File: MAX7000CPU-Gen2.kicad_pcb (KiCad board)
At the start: 2 copper layers, 109 parts, among them J1 Conn_02x05_Odd_Even, J2 Conn_01x08_Male, J4 Conn_01x08_Male, J5 Conn_01x08_Male, J7 Conn_01x05_Male, SW1 SW_Push, SW2 SW_Push, SW3 SW_Push, U1 NE555P, U10 CD4029BEE4, U11 CD4029BEE4, U12 CD4029BEE4, U13 74LS241, U14 74LS241, U15 74LS241, U16 74LS241, U17 74LS574, U18 74LS574, U19 AS6C1008-55PCN, U2 NE555P, U20 74LS574, U21 CD4029BEE4, U22 CD4029BEE4, U23 CD4029BEE4, U24 CD4029BEE4, U25 74LS241, U26 74LS241, U28 74LS574, U29 EPM7128slc84-15n, U3 NE555P, U4 74LS574, U5 74LS574, U6 74LS574, U7 74LS574, U8 74LS574, U9 CD4029BEE4

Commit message: Counter Layout
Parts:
- removed the R2 at (122.0, 28.8)
- removed the U1 at (69.5, 71.1)
- removed the U8 at (20.4, 55.1)
- added R10: 50K, Resistor_THT:R_Axial_DIN0207_L6.3mm_D2.5mm_P7.62mm_Horizontal, F.Cu at (141.8, 78.0)
- added R11: 50K, Resistor_THT:R_Axial_DIN0207_L6.3mm_D2.5mm_P7.62mm_Horizontal, F.Cu at (348.2, 78.0)
- added R12: 50K, Resistor_THT:R_Axial_DIN0207_L6.3mm_D2.5mm_P7.62mm_Horizontal, F.Cu at (335.8, 66.0)
- added R13: 50K, Resistor_THT:R_Axial_DIN0207_L6.3mm_D2.5mm_P7.62mm_Horizontal, F.Cu at (131.1, 90.1)
- added R14: 50K, Resistor_THT:R_Axial_DIN0207_L6.3mm_D2.5mm_P7.62mm_Horizontal, F.Cu at (152.6, 78.0)
- added R15: 50K, Resistor_THT:R_Axial_DIN0207_L6.3mm_D2.5mm_P7.62mm_Horizontal, F.Cu at (376.7, 103.1)
- added R28: 50K, Resistor_THT:R_Axial_DIN0207_L6.3mm_D2.5mm_P7.62mm_Horizontal, F.Cu at (336.6, 95.0)
- added R29: 50K, Resistor_THT:R_Axial_DIN0207_L6.3mm_D2.5mm_P7.62mm_Horizontal, F.Cu at (376.4, 65.8)
- added R30: 50K, Resistor_THT:R_Axial_DIN0207_L6.3mm_D2.5mm_P7.62mm_Horizontal, F.Cu at (141.8, 90.1)
- added R31: 50K, Resistor_THT:R_Axial_DIN0207_L6.3mm_D2.5mm_P7.62mm_Horizontal, F.Cu at (376.4, 94.2)
- added R32: 50K, Resistor_THT:R_Axial_DIN0207_L6.3mm_D2.5mm_P7.62mm_Horizontal, F.Cu at (376.4, 83.8)
- added R33: 50K, Resistor_THT:R_Axial_DIN0207_L6.3mm_D2.5mm_P7.62mm_Horizontal, F.Cu at (141.8, 94.2)
- added R34: 50K, Resistor_THT:R_Axial_DIN0207_L6.3mm_D2.5mm_P7.62mm_Horizontal, F.Cu at (152.6, 86.1)
- added R35: 50K, Resistor_THT:R_Axial_DIN0207_L6.3mm_D2.5mm_P7.62mm_Horizontal, F.Cu at (163.4, 82.0)
- added R36: 50K, Resistor_THT:R_Axial_DIN0207_L6.3mm_D2.5mm_P7.62mm_Horizontal, F.Cu at (152.6, 90.1)
- added R37: 50K, Resistor_THT:R_Axial_DIN0207_L6.3mm_D2.5mm_P7.62mm_Horizontal, F.Cu at (141.8, 98.2)
- added R38: 50K, Resistor_THT:R_Axial_DIN0207_L6.3mm_D2.5mm_P7.62mm_Horizontal, F.Cu at (152.6, 94.2)
- added R39: 50K, Resistor_THT:R_Axial_DIN0207_L6.3mm_D2.5mm_P7.62mm_Horizontal, F.Cu at (152.6, 98.2)
- added R40: 50K, Resistor_THT:R_Axial_DIN0207_L6.3mm_D2.5mm_P7.62mm_Horizontal, F.Cu at (163.4, 86.1)
- added R41: 50K, Resistor_THT:R_Axial_DIN0207_L6.3mm_D2.5mm_P7.62mm_Horizontal, F.Cu at (163.4, 90.1)
- added R42: 50K, Resistor_THT:R_Axial_DIN0207_L6.3mm_D2.5mm_P7.62mm_Horizontal, F.Cu at (359.2, 78.0)
- added R43: 50K, Resistor_THT:R_Axial_DIN0207_L6.3mm_D2.5mm_P7.62mm_Horizontal, F.Cu at (358.9, 118.1)
- added R6: 1K, Resistor_THT:R_Axial_DIN0207_L6.3mm_D2.5mm_P7.62mm_Horizontal, F.Cu at (341.6, 51.8)
- added R8: 50K, Resistor_THT:R_Axial_DIN0207_L6.3mm_D2.5mm_P7.62mm_Horizontal, F.Cu at (131.1, 78.0)
- added R9: 50K, Resistor_THT:R_Axial_DIN0207_L6.3mm_D2.5mm_P7.62mm_Horizontal, F.Cu at (131.1, 82.0)
- added RV1: 1M, MAX7000CPU:SIP460W50P254L970H980Q3P, F.Cu at (328.4, 58.4)
- added U15: 74LS574, Package_DIP:DIP-20_W7.62mm, F.Cu at (324.4, 95.0)
- added U2: NE555P, Package_DIP:DIP-8_W7.62mm, F.Cu at (324.4, 44.4)
- moved U19 368.7 mm to (398.0, 96.8), turned to 180 degrees
- moved U10 318.2 mm to (364.5, 66.0)
- moved U16 306.1 mm to (364.7, 95.0)
- moved C1 303.6 mm to (394.5, 52.5), turned to 90 degrees
- moved U7 297.4 mm to (340.9, 73.4), turned to 90 degrees
- moved C2 297.4 mm to (394.5, 44.2), turned to 270 degrees
- moved R2 286.6 mm to (399.3, 44.7), turned to 270 degrees
- moved U13 284.8 mm to (341.4, 89.9), turned to 90 degrees
- moved C17 279.3 mm to (376.4, 98.8), turned to 270 degrees
- moved C4 277.6 mm to (368.0, 44.2), turned to 270 degrees
- moved R4 275.9 mm to (377.7, 52.3), turned to 90 degrees
- moved U14 272.8 mm to (341.4, 102.4), turned to 90 degrees
- moved SW3 269.9 mm to (372.1, 56.4)
- moved U3 264.8 mm to (355.9, 44.5)
- moved C16 264.0 mm to (368.0, 62.7), turned to 180 degrees
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- renumbered C5 to C1, C14 to C10, C15 to C11, C16 to C12, C17 to C13, C18 to C14, C19 to C15, C20 to C16, C21 to C17, C22 to C18, C23 to C19, C6 to C2, C24 to C20, C25 to C21, C26 to C22, C27 to C23, C28 to C24, C29 to C25, C30 to C26, C31 to C27, C32 to C28, C33 to C29, C34 to C30, C35 to C31, C36 to C32, C37 to C33, C38 to C34, C10 to C35, C9 to C36, C8 to C37, C7 to C38, C1 to C5, C2 to C6, C11 to C7, C12 to C8, C13 to C9, D2 to D1, D11 to D10, D12 to D11, D13 to D12, D14 to D13, D15 to D14, D16 to D15, D17 to D16, D3 to D2, D4 to D3, D5 to D4, D6 to D5, D7 to D6, D8 to D7, D9 to D8, D10 to D9, J4 to J1, J5 to J3, J1 to J4, J7 to J5, R21 to R16, R22 to R17, R12 to R18, R13 to R19, R6 to R2, R14 to R20, R15 to R21, R16 to R22, R17 to R23, R18 to R24, R19 to R25, R23 to R26, R24 to R27, R4 to R3, R5 to R4, R3 to R5, R20 to R7, SW2 to SW1, SW1 to SW2, U3 to U1, U13 to U10, U15 to U11, U16 to U12, U10 to U13, U11 to U14, U14 to U16, U12 to U17, U21 to U18, U25 to U20, U17 to U21, U26 to U24, U18 to U25, U20 to U26, U28 to U27, U24 to U28, U2 to U3, U9 to U7, U29 to U8, U7 to U9
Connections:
- U11 pad 1: GND -> Net-(R13-Pad1)
- U11 pad 19: GND -> Net-(R13-Pad1)
- U12 pad 1: GND -> Net-(R14-Pad1)
- U12 pad 19: GND -> Net-(R14-Pad1)
- U13 pad 10: +5V -> Net-(R42-Pad1)
- U13 pad 9: +5V -> Net-(R43-Pad1)
- U14 pad 10: +5V -> Net-(R42-Pad1)
- U14 pad 9: +5V -> Net-(R43-Pad1)
- U17 pad 10: +5V -> Net-(R42-Pad1)
- U17 pad 9: +5V -> Net-(R43-Pad1)
- U18 pad 5: GND -> Net-(R30-Pad1)
- U19 pad 2: GND -> Net-(R37-Pad2)
- U19 pad 22: GND -> Net-(R36-Pad2)
- U19 pad 30: +5V -> Net-(R31-Pad1)
- U26 pad 1: GND -> Net-(R39-Pad1)
- U27 pad 1: GND -> Net-(R40-Pad1)
- U5 pad 1: GND -> Net-(R9-Pad1)
- U6 pad 1: GND -> Net-(R10-Pad1)
- U7 pad 10: +5V -> Net-(R42-Pad1)
- U7 pad 5: GND -> Net-(R11-Pad1)
- U7 pad 9: +5V -> Net-(R43-Pad1)
- U9 pad 1: GND -> Net-(R12-Pad1)

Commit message: PCB component placements
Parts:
- removed R15, R41: 50K, Resistor_THT:R_Axial_DIN0207_L6.3mm_D2.5mm_P7.62mm_Horizontal
- J4: value Conn_02x05_Odd_Even -> JTAGCON
- moved C17 313.0 mm to (64.7, 70.1), turned to 180 degrees
- moved U19 304.8 mm to (94.0, 74.7)
- moved U16 304.6 mm to (61.0, 73.2)
- moved C10 304.3 mm to (24.6, 41.1)
- moved C11 304.3 mm to (24.6, 70.1)
- moved C12 304.3 mm to (32.3, 55.6)
- moved C13 304.3 mm to (32.3, 60.7)
- moved C14 304.3 mm to (32.3, 67.6)
- moved C15 304.3 mm to (32.3, 85.9)
- moved C5 304.3 mm to (33.1, 30.5)
- moved C6 304.3 mm to (33.1, 24.7)
- moved C7 304.3 mm to (24.6, 19.8)
- moved R1 304.3 mm to (42.9, 22.4)
- moved R12 304.3 mm to (32.3, 44.2)
- moved R2 304.3 mm to (95.8, 22.9)
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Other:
- board outline added: 154.9 x 89.2 mm

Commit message: all parts laid out
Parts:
- removed C34, C37, C38: 100n, Capacitor_SMD:C_0805_2012Metric_Pad1.18x1.45mm_HandSolder
- removed R38: 50K, Resistor_THT:R_Axial_DIN0207_L6.3mm_D2.5mm_P7.62mm_Horizontal
- J4 JTAG: renamed from J4; value JTAGCON -> Conn_02x05_Odd_Even
- moved C33 386.3 mm to (46.8, 96.3)
- moved D7 368.5 mm to (74.7, 114.3), turned to 90 degrees
- moved D3 367.7 mm to (56.4, 114.3), turned to 90 degrees
- moved D6 366.1 mm to (70.1, 114.3), turned to 90 degrees
- moved D9 357.3 mm to (84.8, 114.3), turned to 90 degrees
- moved D4 356.0 mm to (61.0, 114.3), turned to 90 degrees
- moved D1 348.6 mm to (47.2, 114.3), turned to 90 degrees
- moved D5 339.8 mm to (65.5, 114.3), turned to 90 degrees
- moved D12 337.2 mm to (98.6, 114.3), turned to 90 degrees
- moved D2 336.8 mm to (51.8, 114.3), turned to 90 degrees
- moved D10 329.4 mm to (89.4, 114.3), turned to 90 degrees
- moved R14 317.4 mm to (125.2, 107.4), turned to 270 degrees
- moved C36 307.3 mm to (101.9, 95.0), turned to 270 degrees
- moved R17 304.2 mm to (91.4, 106.4), turned to 180 degrees
- moved R40 303.3 mm to (149.6, 97.3), turned to 270 degrees
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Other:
- board size 154.9 x 89.2 mm -> 154.9 x 99.3 mm
- board text added: "+5V"
- board text added: "CLK"
- board text added: "GND"
- board text added: "SNC"
- board text added: "STT"

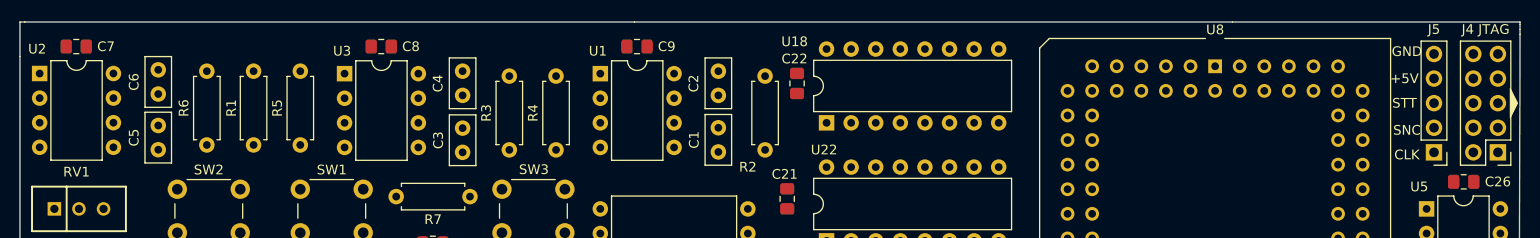
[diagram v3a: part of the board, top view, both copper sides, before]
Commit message: silk screening - clock module
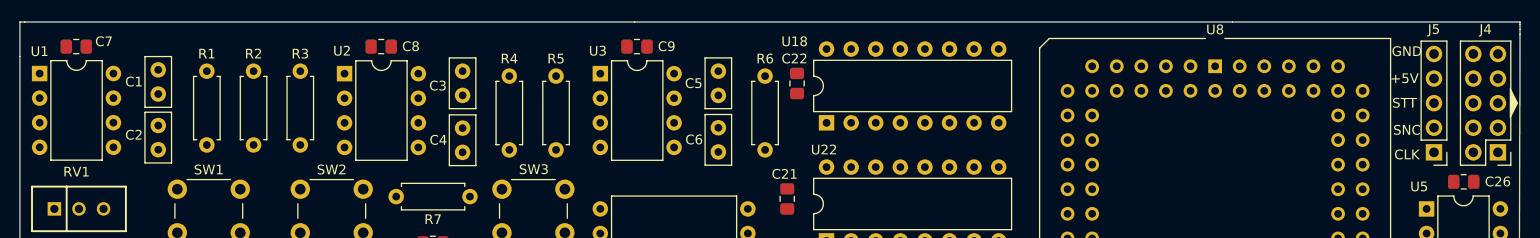
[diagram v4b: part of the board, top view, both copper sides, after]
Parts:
- removed the R2 at (95.8, 22.9)
- added R6: 1M, Resistor_THT:R_Axial_DIN0207_L6.3mm_D2.5mm_P7.62mm_Horizontal, F.Cu at (95.8, 22.9)
- J4: renamed from J4 JTAG
- renumbered C6 to C1, C5 to C2, C4 to C3, C3 to C4, C2 to C5, C1 to C6, R6 to R1, R1 to R2, R5 to R3, R3 to R4, R4 to R5, SW2 to SW1, SW1 to SW2, U2 to U1, U3 to U2, U1 to U3

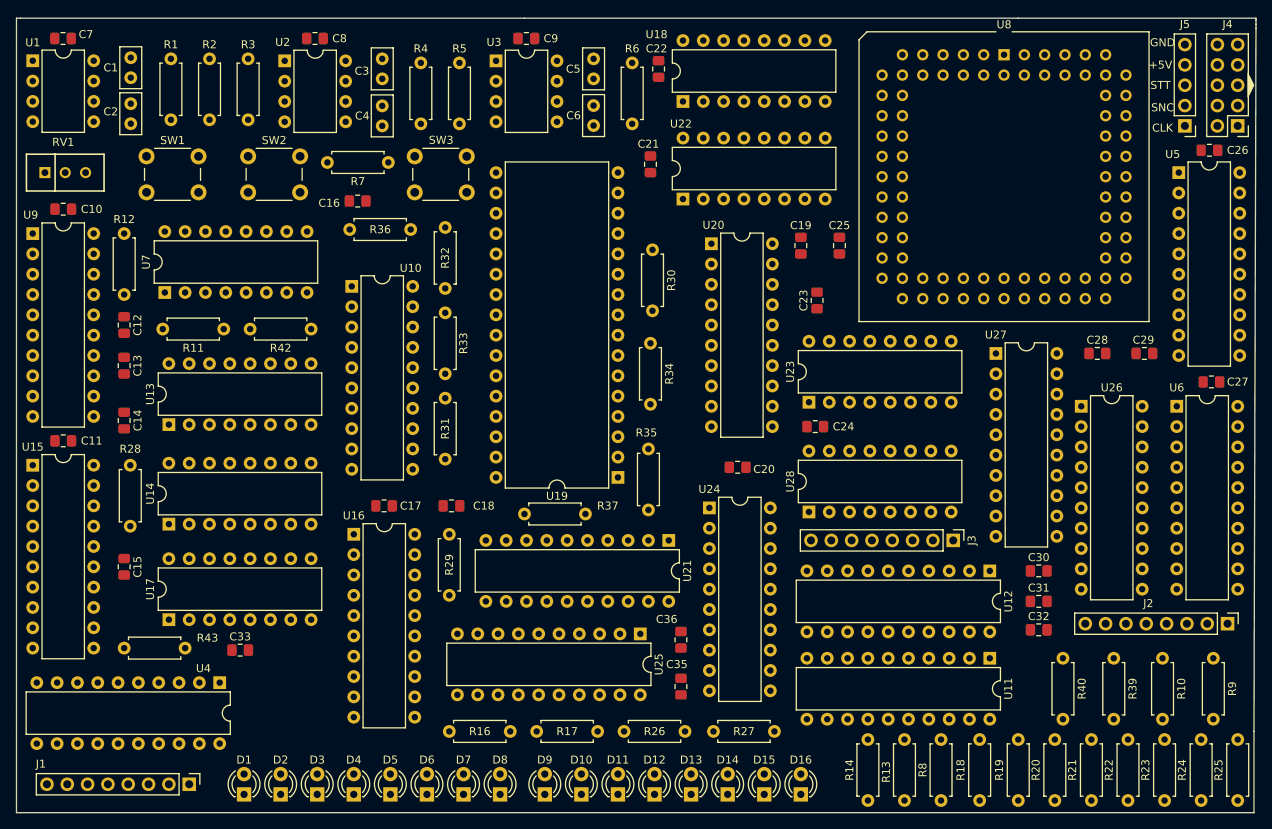
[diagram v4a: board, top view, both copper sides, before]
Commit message: silkscreening and 3d models implemented
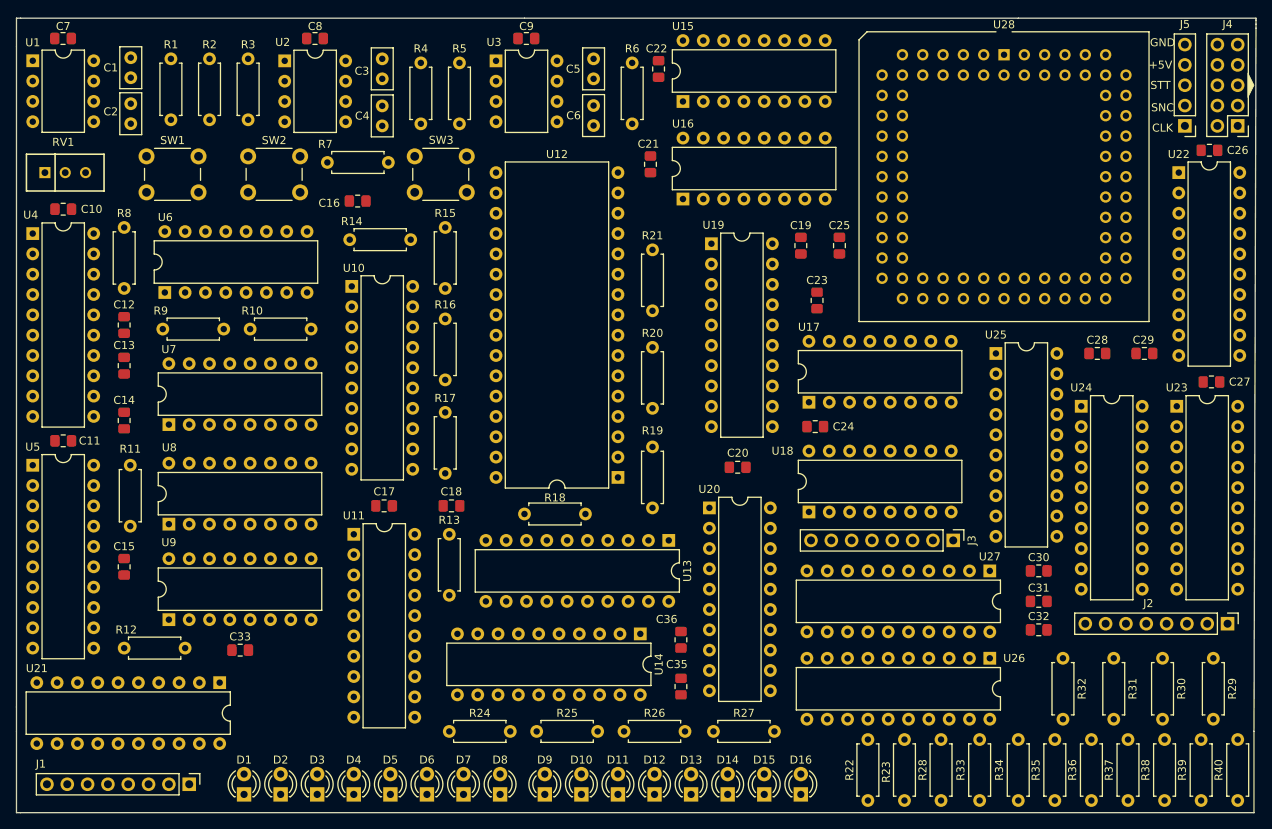
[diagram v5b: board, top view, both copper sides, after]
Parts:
- removed the R33 at (72.4, 61.7)
- added R16: 50K, Resistor_THT:R_Axial_DIN0207_L6.3mm_D2.5mm_P7.62mm_Horizontal, F.Cu at (72.4, 62.5)
- moved R17 1.78 mm to (72.4, 74.2)
- moved R14 1.27 mm to (60.5, 45.0)
- moved R8 0.76 mm to (32.3, 43.4)
- moved R20 0.57 mm to (98.3, 58.4)
- moved R19 0.57 mm to (98.3, 78.5)
- renumbered R42 to R10, R28 to R11, R43 to R12, R29 to R13, R36 to R14, R32 to R15, R31 to R17, R37 to R18, R35 to R19, R34 to R20, R30 to R21, R14 to R22, R13 to R23, R16 to R24, R17 to R25, R8 to R28, R9 to R29, R10 to R30, R39 to R31, R40 to R32, R18 to R33, R19 to R34, R20 to R35, R21 to R36, R22 to R37, R23 to R38, R24 to R39, R25 to R40, R12 to R8, R11 to R9, U16 to U11, U19 to U12, U21 to U13, U25 to U14, U18 to U15, U22 to U16, U23 to U17, U28 to U18, U20 to U19, U24 to U20, U4 to U21, U5 to U22, U6 to U23, U26 to U24, U27 to U25, U11 to U26, U12 to U27, U8 to U28, U9 to U4, U15 to U5, U7 to U6, U13 to U7, U14 to U8, U17 to U9

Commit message: traces routed
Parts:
- removed C36: 100n, Capacitor_SMD:C_0805_2012Metric_Pad1.18x1.45mm_HandSolder
- added C34: 100n, Capacitor_SMD:C_0805_2012Metric_Pad1.18x1.45mm_HandSolder, F.Cu at (102.1, 95.0)
- moved C19 88.3 mm to (44.7, 96.5), turned to 0 degrees
- moved C33 77.5 mm to (118.9, 68.1)
- moved C24 22.7 mm to (117.3, 45.7), turned to 270 degrees
- moved J3 0.51 mm to (135.9, 83.1)
- moved J2 0.51 mm to (170.2, 93.5)
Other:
- board text added: "Clock Speed"
- board text added: "Instruction"
- board text added: "Main Bus"
- board text added: "Output"
- board text added: "Pause"
- board text added: "Reset"
- board text added: "Step"
- board text added: "What Should Go Here"

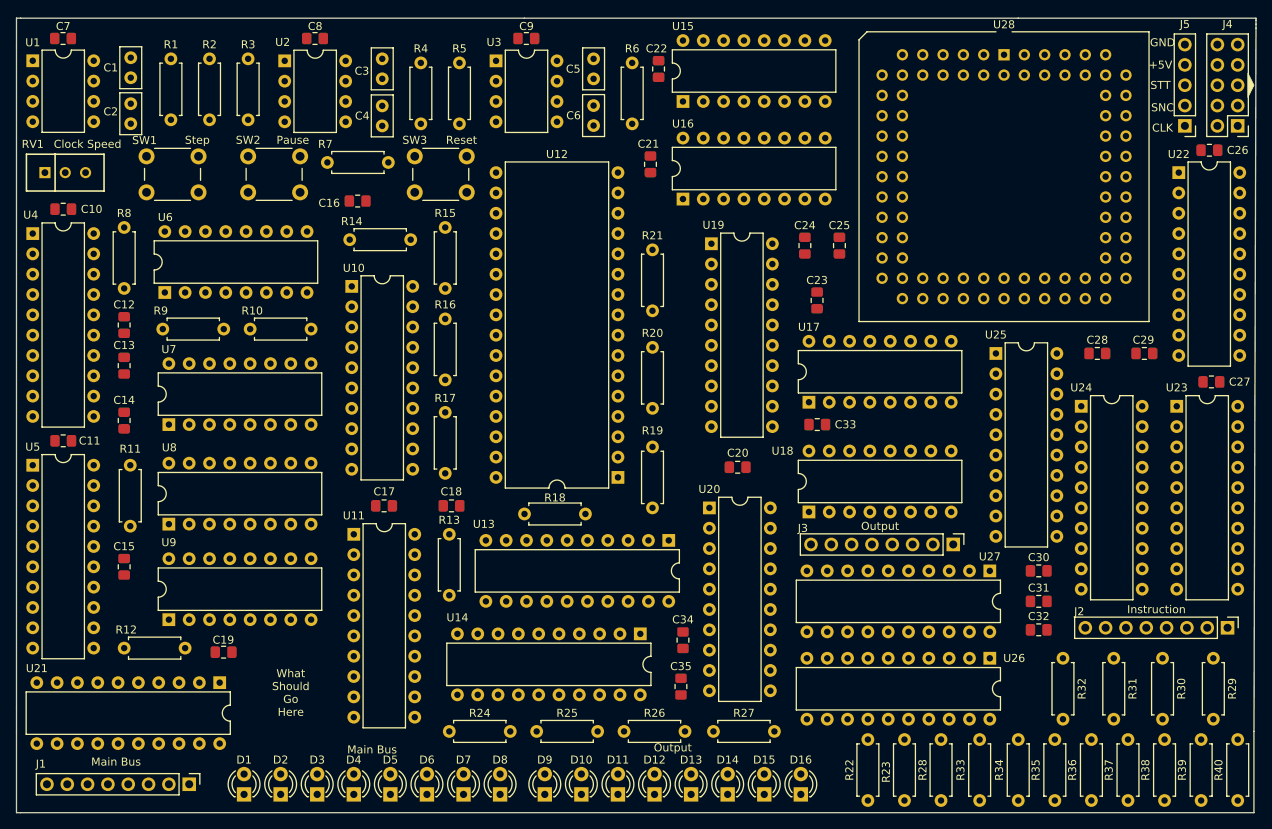
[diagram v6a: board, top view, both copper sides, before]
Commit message: first pass from the autorouter
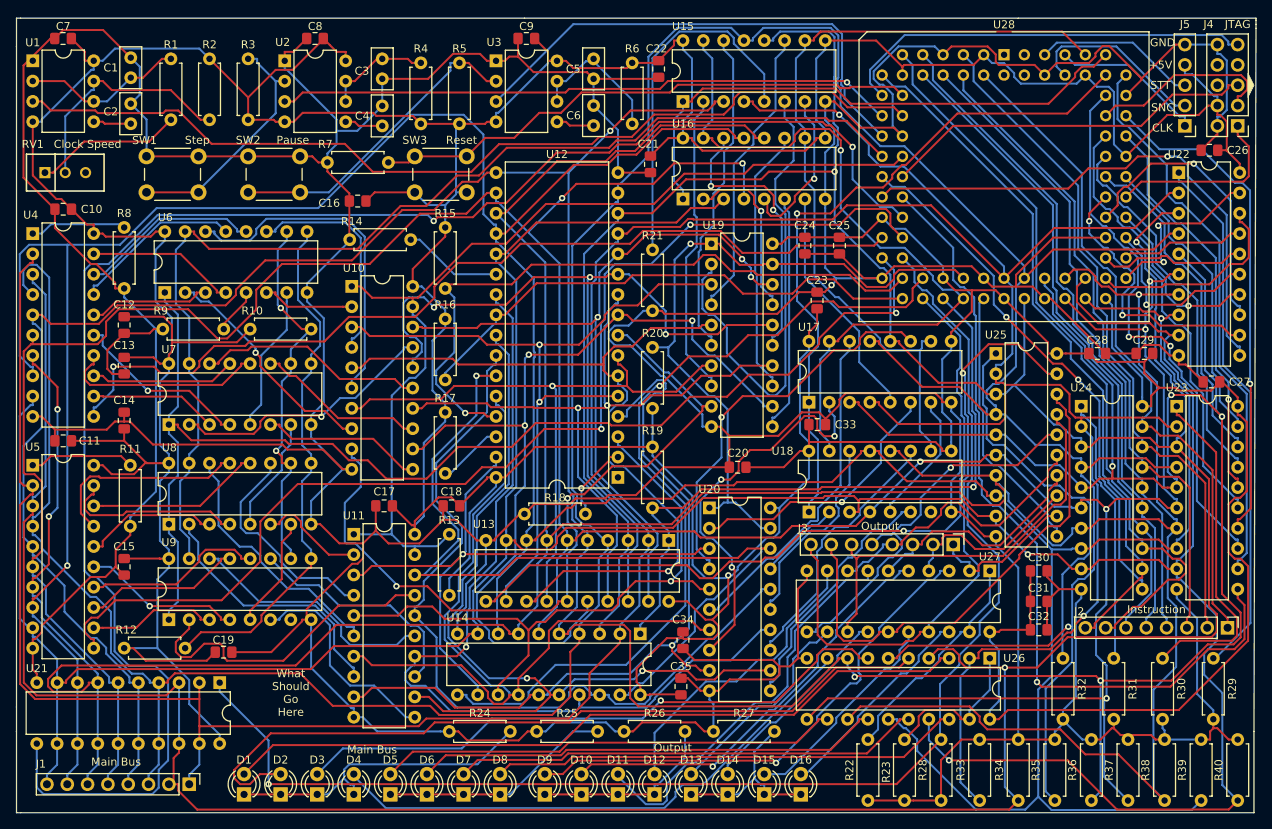
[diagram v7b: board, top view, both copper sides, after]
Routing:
- net GND: track 0.00 -> 1009.0 mm, vias 0 -> 1
- net +5V: track 0.00 -> 902.3 mm, vias 0 -> 1
- net /B1: track 0.00 -> 507.6 mm, vias 0 -> 3
- net /B3: track 0.00 -> 490.6 mm, vias 0 -> 6
- net /B6: track 0.00 -> 474.3 mm, vias 0 -> 2
- net /B5: track 0.00 -> 465.1 mm, vias 0 -> 3
- net /B0: track 0.00 -> 458.6 mm, vias 0 -> 2
- net /B2: track 0.00 -> 453.0 mm, vias 0 -> 1
- net /B4: track 0.00 -> 441.7 mm, vias 0 -> 7
- net /B7: track 0.00 -> 415.8 mm, vias 0 -> 2
- net MainRegReadControl: track 0.00 -> 211.1 mm, vias 0 -> 2
- net MainRegOutputControl: track 0.00 -> 170.6 mm, vias 0 -> 1
- net JumpEnable: track 0.00 -> 154.6 mm, vias 0 -> 1
- net HIGHJumpRegLoad: track 0.00 -> 143.8 mm, vias 0 -> 2
- net Count: track 0.00 -> 140.9 mm
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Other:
- board text added: "JTAG"

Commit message: optimising traces
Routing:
- net GND: track 1009.0 -> 1027.7 mm
- net +5V: track 902.3 -> 919.2 mm
- net /B0: track 458.6 -> 462.5 mm
- net /B4: track 441.7 -> 438.0 mm
- net Net-(D1-Pad1): track 40.0 -> 42.5 mm
- net /B6: track 474.3 -> 472.5 mm
- net CounterOutControl: track 123.5 -> 125.1 mm
- net /B2: track 453.0 -> 451.5 mm
- net Net-(D13-Pad1): track 23.0 -> 24.5 mm
- net /B3: track 490.6 -> 489.2 mm
- net /B5: track 465.1 -> 463.9 mm
- net StackOutControl: track 86.4 -> 87.6 mm
- net /B7: track 415.8 -> 414.6 mm
- net /Qo0: track 18.9 -> 17.9 mm
- net /Ins7: track 87.3 -> 86.4 mm
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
